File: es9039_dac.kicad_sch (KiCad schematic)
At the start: 22 parts, among them U1 ES9039Q2M, U2 TPS7A2033DBV, U3 TPS7A2033DBV

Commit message: some changes
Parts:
- added J1: Conn_02x07_Odd_Even, Connector_IDC:IDC-Header_2x07_P2.54mm_Vertical, symbol Connector_Generic:Conn_02x07_Odd_Even
- added R5: 0, Resistor_SMD:R_0603_1608Metric, symbol Device:R_Small
- C1, C2, C3, C4, C8: footprint Capacitor_SMD:C_0805_2012Metric -> Capacitor_SMD:C_0603_1608Metric
- R1, R2: footprint Resistor_SMD:R_1206_3216Metric -> Resistor_SMD:R_0805_2012Metric
- R3, R4: footprint Resistor_SMD:R_0805_2012Metric -> Resistor_SMD:R_0603_1608Metric
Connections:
- net GNDA: now also U1.33 (EP), J1.6 (Pin_6), J1.8 (Pin_8), R5.2
- net GNDD: now also U1.30 (GND), J1.2 (Pin_2), J1.4 (Pin_4), R5.1
- net MCU_EN_DAC renamed STBY
- net STBY: now also J1.11 (Pin_11)
- net VCC renamed +5V
- net +5V: now also J1.12 (Pin_12)
- new net +12V: J1.13 (Pin_13)
- new net -12V: J1.14 (Pin_14)
- new net BCLK: J1.3 (Pin_3)
- new net DATA: J1.7 (Pin_7)
- new net I2C_SCL: J1.10 (Pin_10)
- new net I2C_SDA: J1.9 (Pin_9)
- new net LRCK: J1.5 (Pin_5)
- new net MCLK: J1.1 (Pin_1)

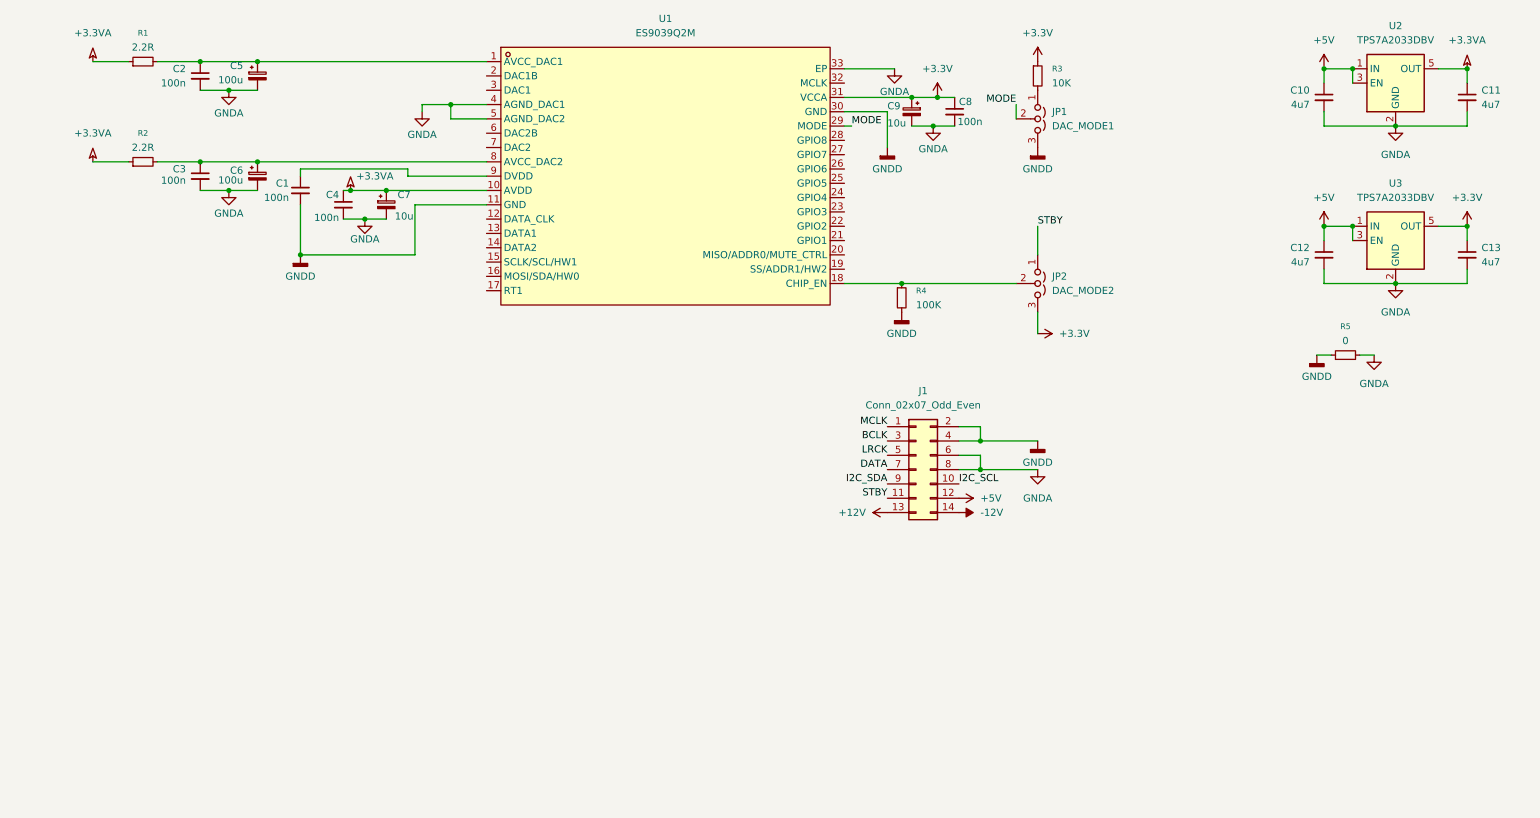
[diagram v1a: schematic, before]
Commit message: deleted pcb and some changes in schematic
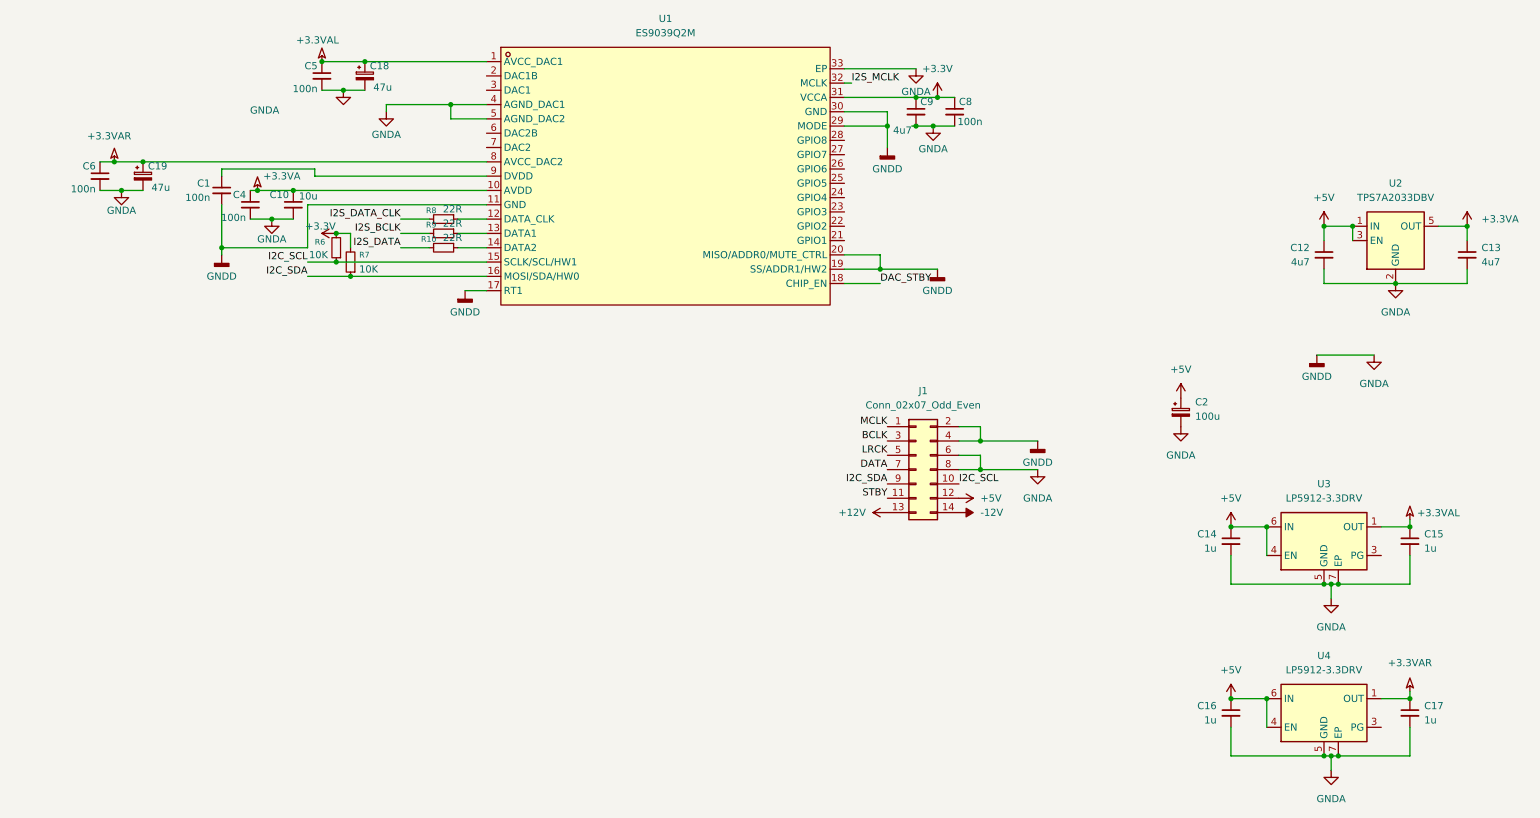
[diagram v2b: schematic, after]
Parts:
- removed C11: 4u7, Capacitor_SMD:C_0805_2012Metric, symbol Device:C_Small
- removed C2, C3: 100n, Capacitor_SMD:C_0603_1608Metric, symbol Device:C_Small
- removed C5, C6: 100u, Capacitor_SMD:CP_Elec_6.3x5.8, symbol Device:C_Polarized_Small
- removed C7, C9: 10u, Capacitor_SMD:CP_Elec_4x5.4, symbol Device:C_Polarized_Small
- removed JP1: DAC_MODE1, Connector_PinHeader_2.54mm:PinHeader_1x03_P2.54mm_Vertical, symbol Jumper:Jumper_3_Open
- removed JP2: DAC_MODE2, Connector_PinHeader_2.54mm:PinHeader_1x03_P2.54mm_Vertical, symbol Jumper:Jumper_3_Open
- removed R1, R2: 2.2R, Resistor_SMD:R_0805_2012Metric, symbol Device:R_Small
- removed R3: 10K, Resistor_SMD:R_0603_1608Metric, symbol Device:R_Small
- removed R4: 100K, Resistor_SMD:R_0603_1608Metric, symbol Device:R_Small
- removed R5: 0, Resistor_SMD:R_0603_1608Metric, symbol Device:R_Small
- removed U2: TPS7A2033DBV, Package_TO_SOT_SMD:SOT-23-5, symbol Regulator_Linear:TPS7A20xxxDBV
- added C14, C15, C16, C17: 1u, Capacitor_SMD:C_0603_1608Metric, symbol Device:C_Small
- added C18, C19: 47u, Capacitor_Tantalum_SMD:CP_EIA-3528-12_Kemet-T, symbol Device:C_Polarized_Small
- added C2: 100u, Capacitor_SMD:CP_Elec_6.3x5.8, symbol Device:C_Polarized_Small
- added C5, C6: 100n, Capacitor_SMD:C_0603_1608Metric, symbol Device:C_Small
- added C9: 4u7, Capacitor_SMD:C_0603_1608Metric, symbol Device:C_Small
- added R10, R8, R9: 22R, Resistor_SMD:R_0603_1608Metric, symbol Device:R_Small
- added R6, R7: 10K, Resistor_SMD:R_0603_1608Metric, symbol Device:R_Small
- added U3, U4: LP5912-3.3DRV, Package_SON:WSON-6-1EP_2x2mm_P0.65mm_EP1x1.6mm_ThermalVias, symbol Regulator_Linear:LP5912-3.3DRV
- C10: value 4u7 -> 10u; footprint Capacitor_SMD:C_0805_2012Metric -> Capacitor_SMD:C_0603_1608Metric
- C12, C13: footprint Capacitor_SMD:C_0805_2012Metric -> Capacitor_SMD:C_0603_1608Metric
- renumbered U3 to U2
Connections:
- net GNDD is gone; now on net GNDA: C1.2, J1.2 (Pin_2), J1.4 (Pin_4), U1.11 (GND), U1.30 (GND)
- net MODE is gone; now on net GNDA: U1.29 (MODE)
- net +3.3V: now also C9.1, R6.2, R7.2; no longer C13.1, U2.5 (OUT)
- net +3.3VA: now also C10.1, C13.1, U2.5 (OUT)
- net +5V: now also C14.1, C16.1, C2.1, U3.4 (EN), U3.6 (IN), U4.4 (EN), U4.6 (IN); no longer C10.1
- net GNDA: now also U1.17 (RT1), U1.19 (SS/ADDR1/HW2), U1.20 (MISO/ADDR0/MUTE_CTRL), C14.2, C15.2, C16.2, C17.2, C18.2, C19.2, C2.2, C5.2, C6.2, C9.2, U3.5 (GND), U3.7 (EP), U4.5 (GND), U4.7 (EP)
- net I2C_SCL: now also U1.15 (SCLK/SCL/HW1), R6.1
- net I2C_SDA: now also U1.16 (MOSI/SDA/HW0), R7.1
- net +3.3VAR: now reaches U1.8 (AVCC_DAC2)
- net +3.3VAR: now also C17.1, C19.1, C6.1, U4.1 (OUT)
- net +3.3VAL: now reaches U1.1 (AVCC_DAC1)
- net +3.3VAL: now also C15.1, C18.1, C5.1, U3.1 (OUT)
- net at U1.12 (DATA_CLK): now also R8.1
- net at U1.13 (DATA1): now also R9.1
- net at U1.14 (DATA2): now also R10.1
- net DAC_STBY: now reaches U1.18 (CHIP_EN)
- net I2S_MCLK: now reaches U1.32 (MCLK)
- new net I2S_BCLK: R9.2
- new net I2S_DATA: R10.2
- new net I2S_DATA_CLK: R8.2
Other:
- moved on the sheet: C1, C4

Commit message: trace dac chip and add output stage
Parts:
- added C20, C21: 4u7, Capacitor_SMD:C_0603_1608Metric, symbol Device:C_Small
- added R11: 22R, Resistor_SMD:R_0603_1608Metric, symbol Device:R_Small
- added U5: TPS7A2033DBV, Package_TO_SOT_SMD:SOT-23-5, symbol Regulator_Linear:TPS7A20xxxDBV
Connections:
- net BCLK is gone; now on net I2S_DATA: J1.3 (Pin_3)
- net DATA is gone; now on net I2S_BCLK: J1.7 (Pin_7)
- net I2S_DATA_CLK is gone; now on net I2S_BCLK: R8.2
- net MCLK is gone; now on net I2S_MCLK: J1.1 (Pin_1)
- net STBY is gone; now on net DAC_STBY: J1.11 (Pin_11)
- net +3.3V: now also C21.1, U5.5 (OUT)
- net +5V: now also C20.1, U5.1 (IN), U5.3 (EN)
- net GNDA: now also C20.2, C21.2, U5.2 (GND)
- net I2S_BCLK: no longer R9.2
- net I2S_MCLK: now also R11.1; no longer U1.32 (MCLK)
- net DAC1B: now reaches U1.2 (DAC1B)
- net DAC1: now reaches U1.3 (DAC1)
- net DAC2B: now reaches U1.6 (DAC2B)
- net DAC2: now reaches U1.7 (DAC2)
- net LRCK renamed I2S_LRCK
- net I2S_LRCK: now also R9.2
- new net: R11.2, U1.32 (MCLK)

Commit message: add rca
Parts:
- U1: footprint EasyEDA:QFN-32_L5.0-W5.0-P0.50-TL-EP3.2 -> Package_DFN_QFN:QFN-32-1EP_5x5mm_P0.5mm_EP3.1x3.1mm_ThermalVias
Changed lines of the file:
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@@
 			)
 		)
-		(property "Footprint" "EasyEDA:QFN-32_L5.0-W5.0-P0.50-TL-EP3.2"
+		(property "Footprint" "Package_DFN_QFN:QFN-32-1EP_5x5mm_P0.5mm_EP3.1x3.1mm_ThermalVias"
 			(at 124.46 80.01 0)
 			(hide yes)

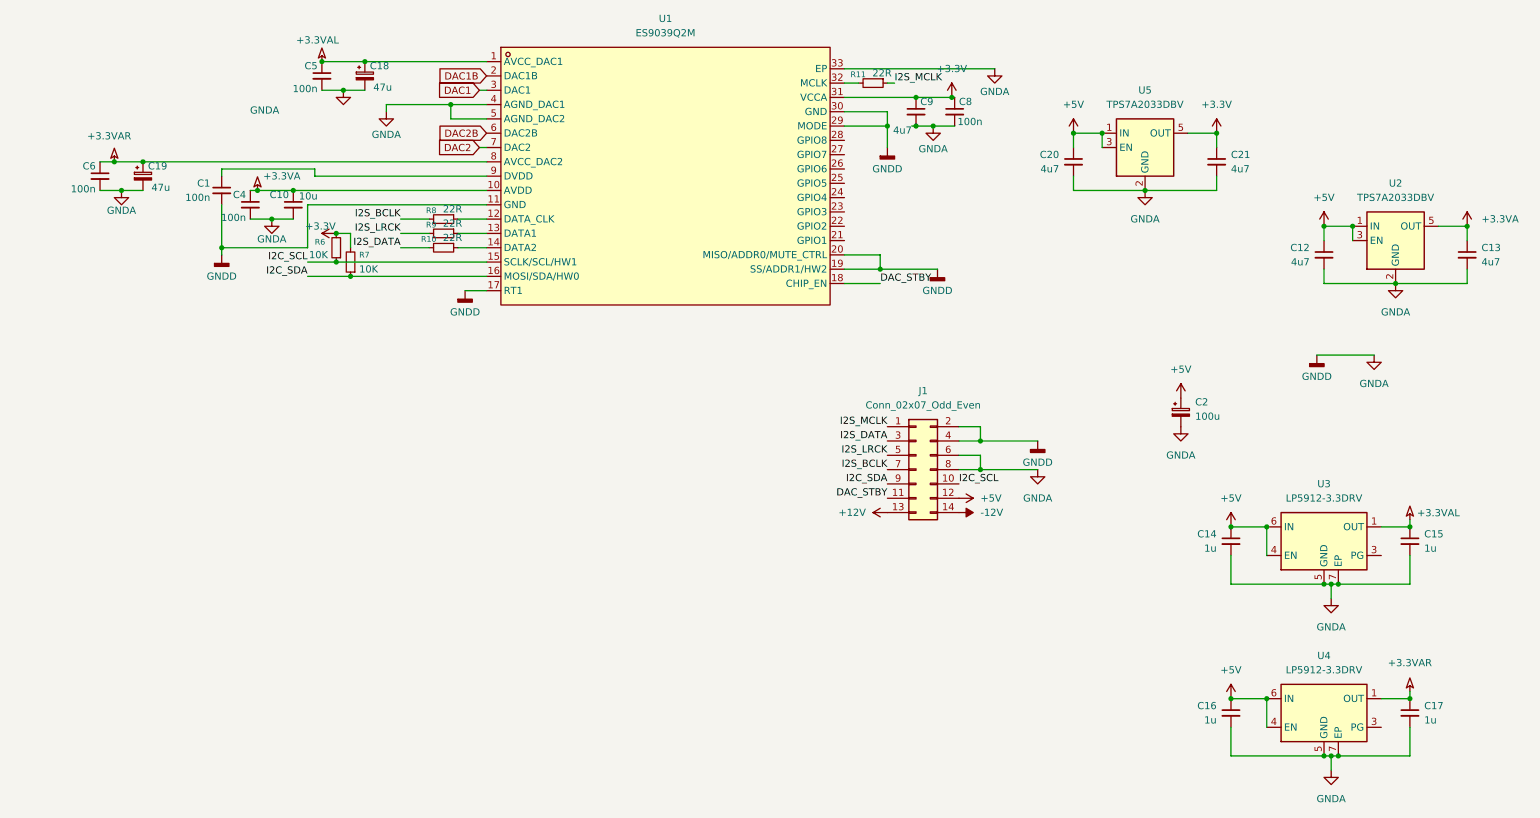
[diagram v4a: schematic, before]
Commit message: add oscillator
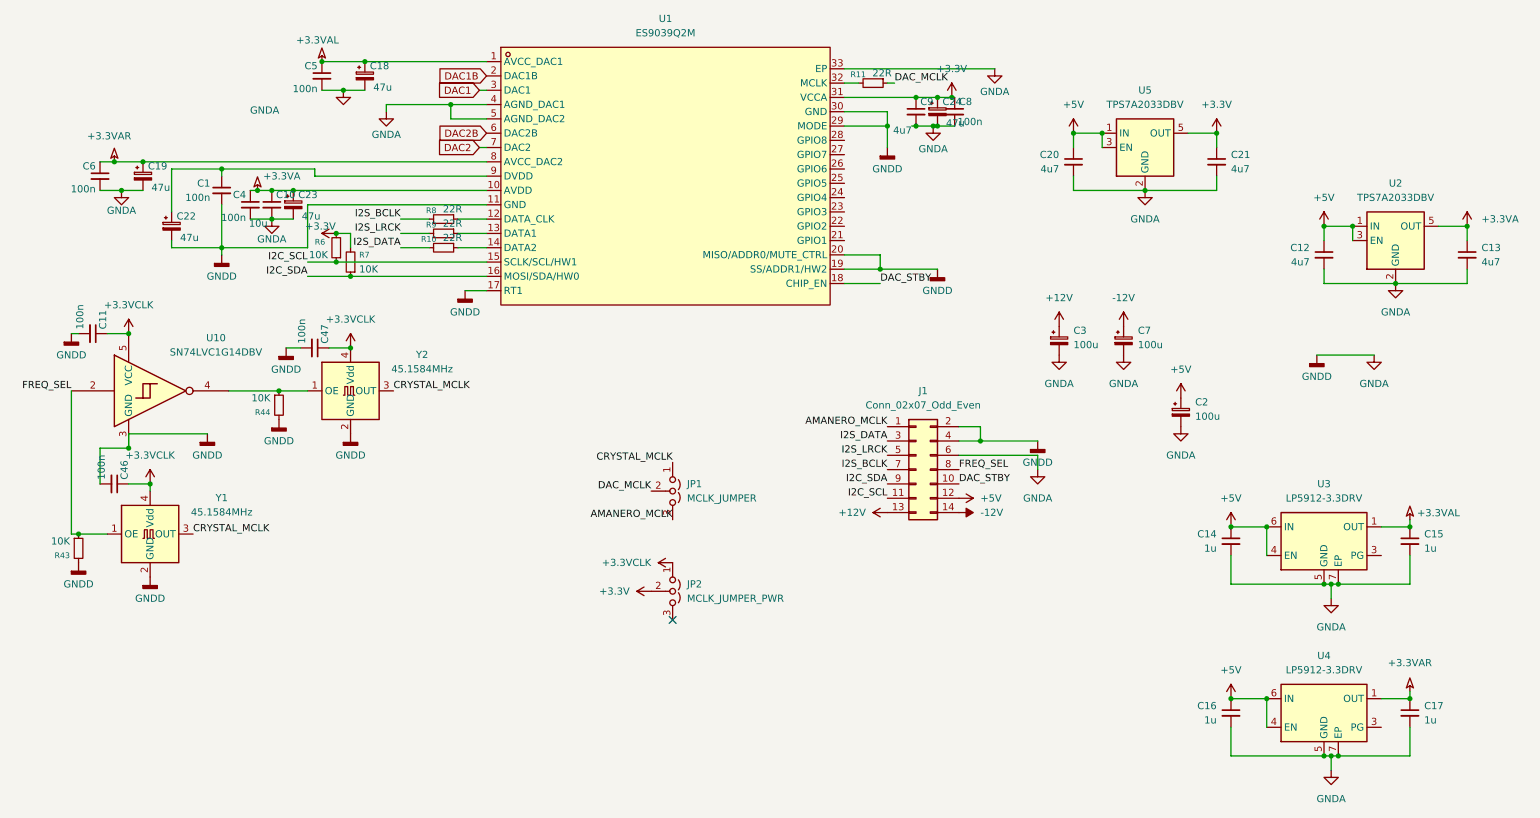
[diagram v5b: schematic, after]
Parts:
- added C11, C46, C47: 100n, Capacitor_SMD:C_0603_1608Metric, symbol Device:C_Small
- added C22, C23, C24: 47u, Capacitor_Tantalum_SMD:CP_EIA-3528-12_Kemet-T, symbol Device:C_Polarized_Small
- added C3, C7: 100u, Capacitor_SMD:CP_Elec_6.3x5.8, symbol Device:C_Polarized_Small
- added JP1: MCLK_JUMPER, Connector_PinHeader_2.54mm:PinHeader_1x03_P2.54mm_Vertical, symbol Jumper:Jumper_3_Open
- added JP2: MCLK_JUMPER_PWR, Connector_PinHeader_2.54mm:PinHeader_1x03_P2.54mm_Vertical, symbol Jumper:Jumper_3_Open
- added R43, R44: 10K, Resistor_SMD:R_0603_1608Metric, symbol Device:R_Small
- added U10: SN74LVC1G14DBV, Package_TO_SOT_SMD:SOT-23-5, symbol 74xGxx:SN74LVC1G14DBV
- added Y1, Y2: 45.1584MHz, Oscillator:Oscillator_SMD_SiT_PQFN-4Pin_2.5x2.0mm, symbol Oscillator:SiT8008xx-1x-xxE
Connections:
- net +12V: now also C3.1
- net +3.3V: now also C24.1, JP2.2 (C)
- net +3.3VA: now also C23.1
- net -12V: now also C7.1
- net DAC_STBY: now also J1.10 (Pin_10); no longer J1.11 (Pin_11)
- net GNDA: now also C11.2, C22.2, C23.2, C24.2, C3.2, C46.2, C47.2, C7.2, R43.2, R44.2, U10.3 (GND), Y1.2 (GND), Y2.2 (GND); no longer J1.8 (Pin_8)
- net I2C_SCL: now also J1.11 (Pin_11); no longer J1.10 (Pin_10)
- net at C1.1, U1.9 (DVDD): now also C22.1
- net I2S_MCLK renamed AMANERO_MCLK
- net AMANERO_MCLK: now also JP1.3 (B); no longer R11.1
- new net: R44.1, U10.4, Y2.1 (OE)
- new net +3.3VCLK: C11.1, C46.1, C47.1, JP2.1 (A), U10.5 (VCC), Y1.4 (Vdd), Y2.4 (Vdd)
- new net CRYSTAL_MCLK: JP1.1 (A), Y1.3 (OUT), Y2.3 (OUT)
- new net DAC_MCLK: JP1.2 (C), R11.1
- new net FREQ_SEL: J1.8 (Pin_8), R43.1, U10.2, Y1.1 (OE)
- no-connect marks 0 -> 1
